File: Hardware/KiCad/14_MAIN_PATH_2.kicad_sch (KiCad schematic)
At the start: 0 parts

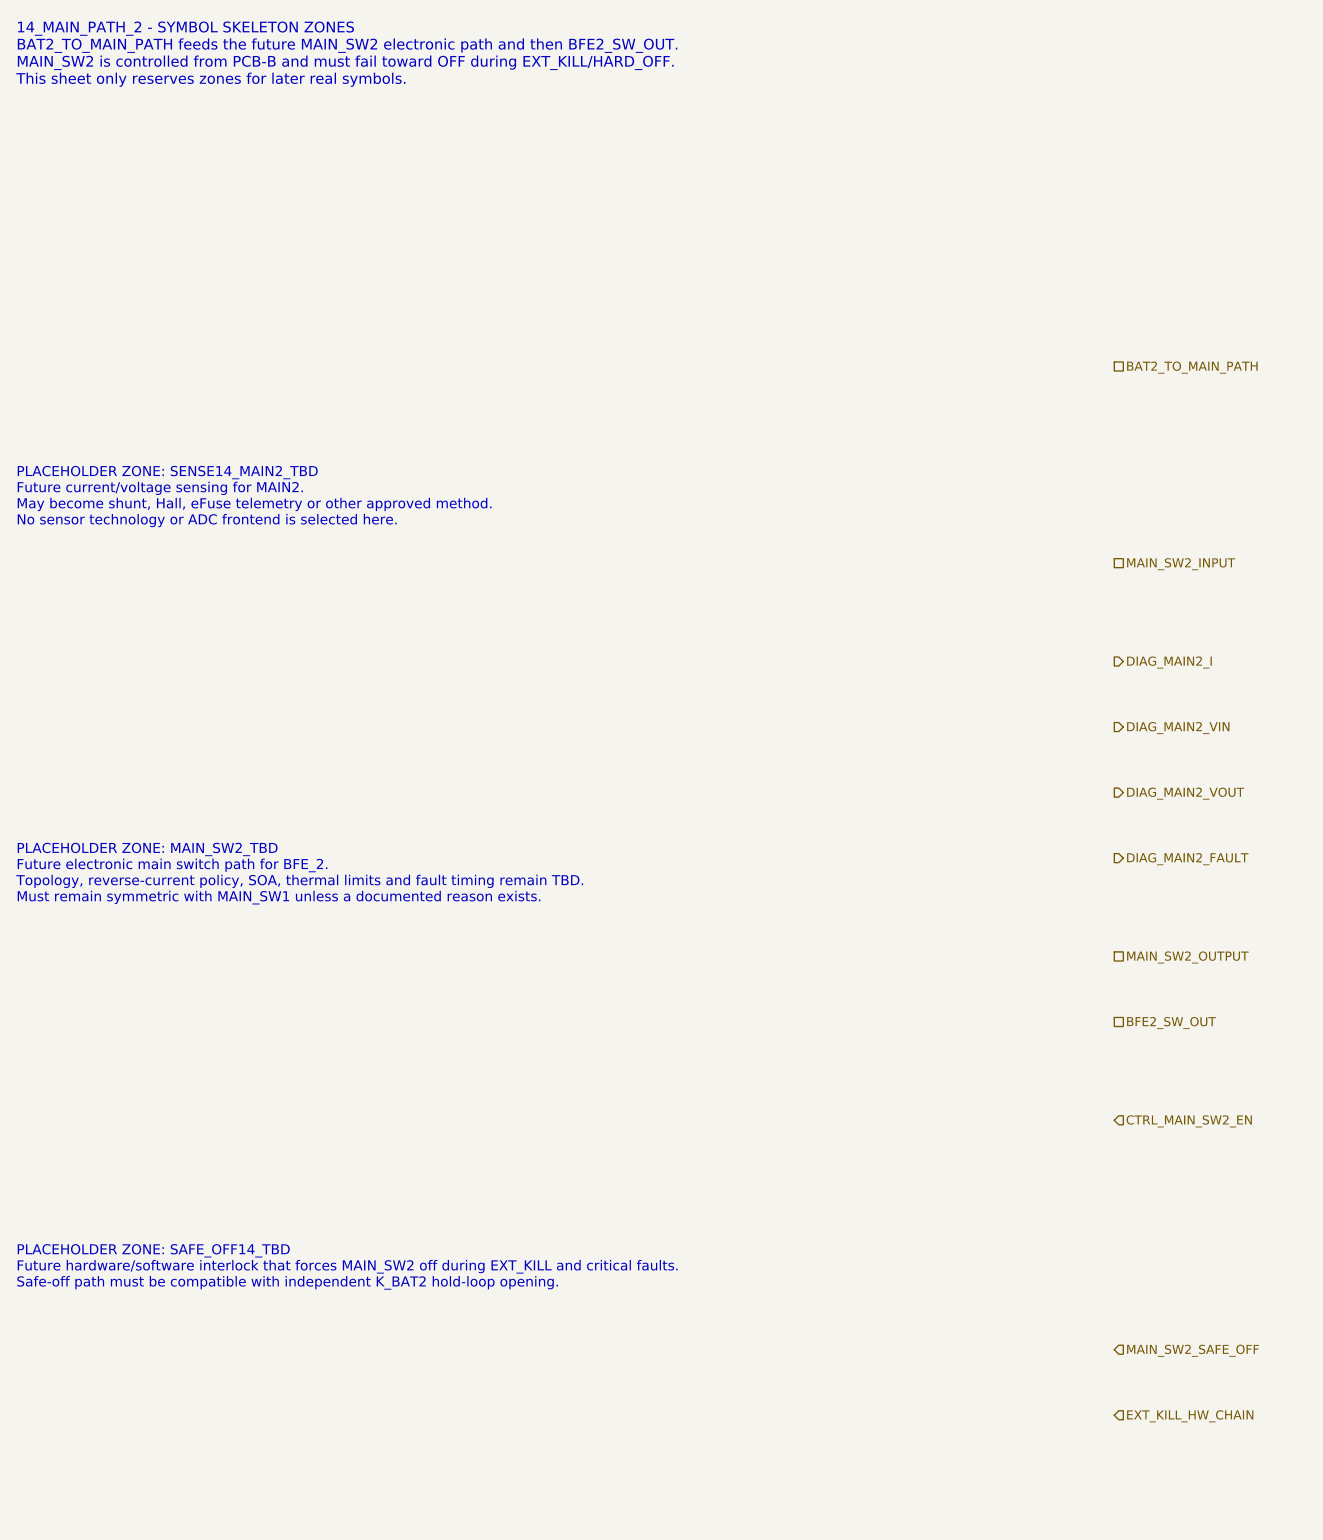
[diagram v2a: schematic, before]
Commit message: hardware: align PCB-B CTRL_RESERVE interfaces
Merge PCB-B interface consistency fixes after verifying canonical names, diagnostics, and independent EXT_KILL final actions.
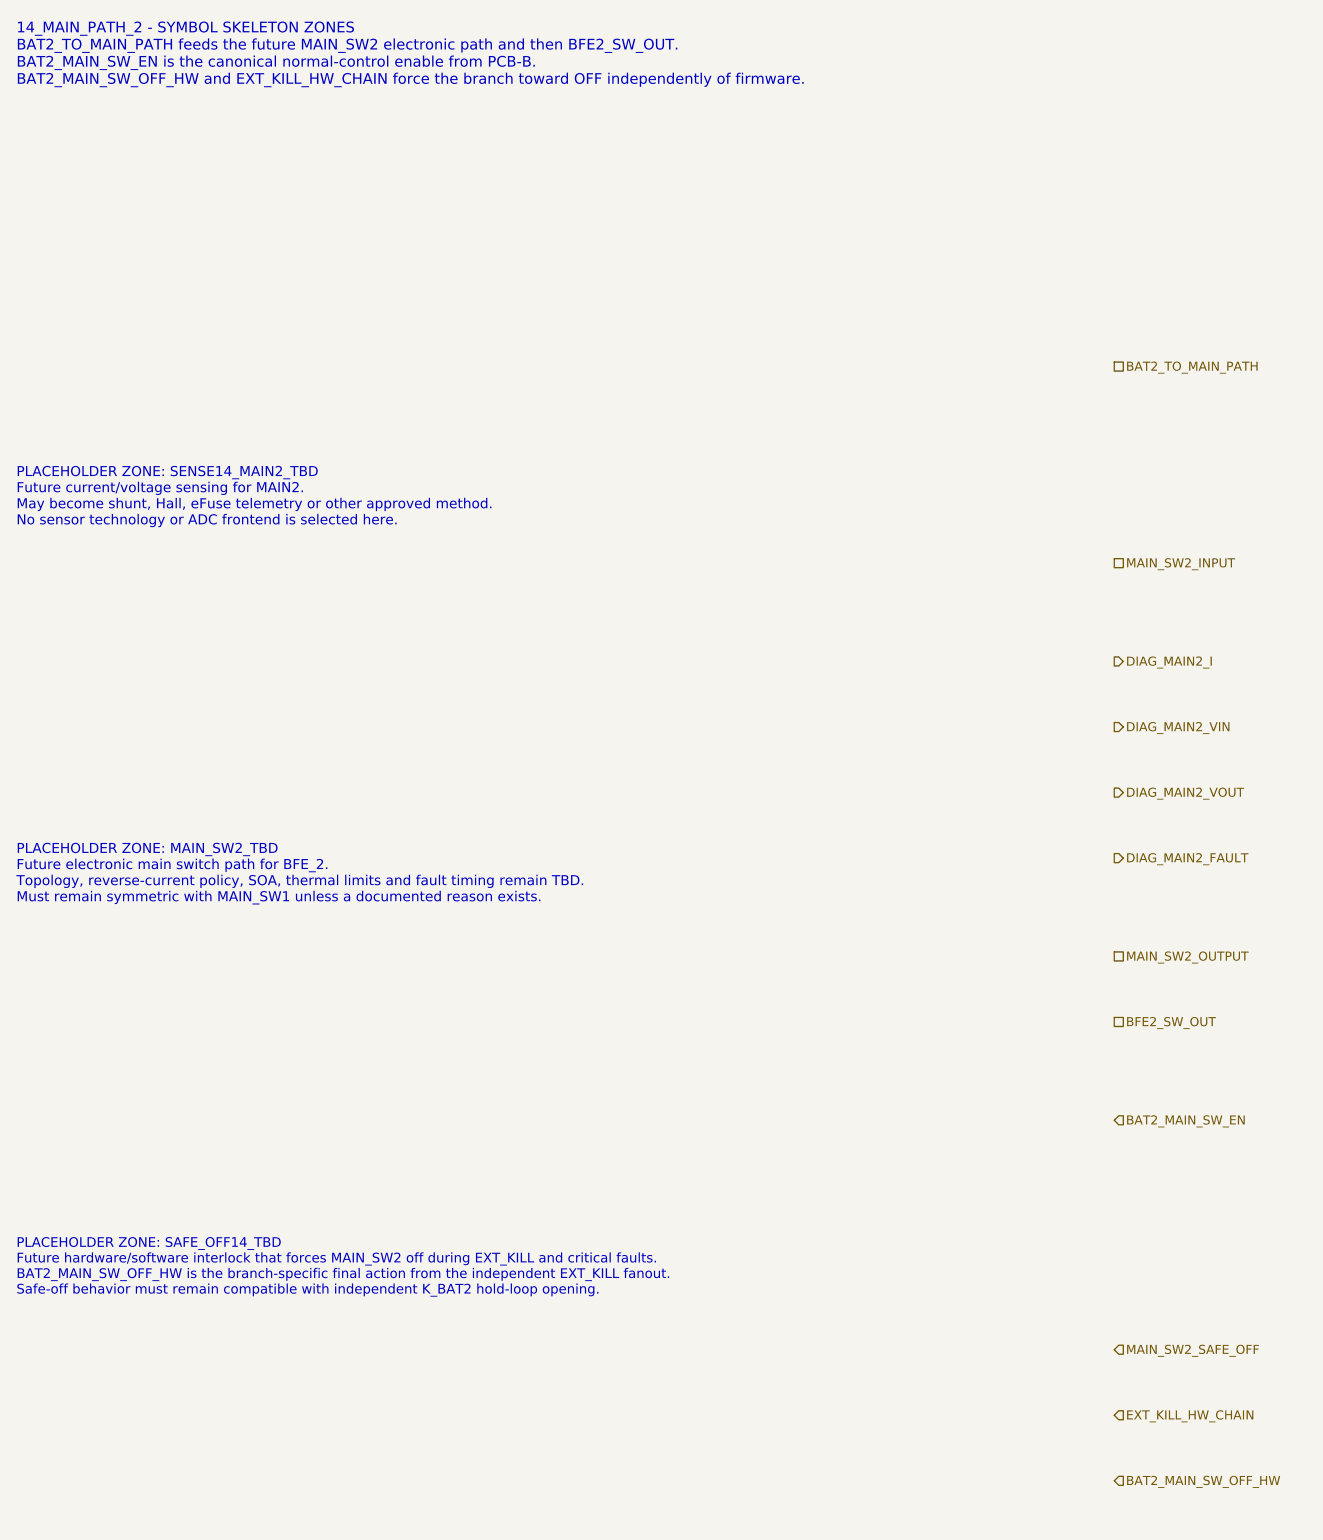
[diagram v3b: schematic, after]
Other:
- note added: "14_MAIN_PATH_2 - SYMBOL SKELETON ZONES BAT2_TO_MAIN_PATH feeds the future MAIN_SW2 electronic path and then BFE2_SW_OUT. BAT2_MAIN_SW_EN is the canonical normal-control enable from PCB-B. BAT2_MAIN_SW_OFF_HW and EXT_KILL_HW_CHAIN force the branch toward OFF independently of firmware."
- note added: "PLACEHOLDER ZONE: SAFE_OFF14_TBD Future hardware/software interlock that forces MAIN_SW2 off during EXT_KILL and critical faults. BAT2_MAIN_SW_OFF_HW is the branch-specific final action from the independent EXT_KILL fanout. Safe-off behavior must remain compatible with independent K_BAT2 hold-loop opening."
- note removed: "14_MAIN_PATH_2 - SYMBOL SKELETON ZONES BAT2_TO_MAIN_PATH feeds the future MAIN_SW2 electronic path and then BFE2_SW_OUT. MAIN_SW2 is controlled from PCB-B and must fail toward OFF during EXT_KILL/HARD_OFF. This sheet only reserves zones for later real symbols."
- note removed: "PLACEHOLDER ZONE: SAFE_OFF14_TBD Future hardware/software interlock that forces MAIN_SW2 off during EXT_KILL and critical faults. Safe-off path must be compatible with independent K_BAT2 hold-loop opening."
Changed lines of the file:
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@@
 		(title "14_MAIN_PATH_2 - BFE_2 main electronic path")
 		(date "2026-07-15")
-		(rev "C1")
+		(rev "C2")
 		(company "Gonoboben/plataVM")
-		(comment 1 "Symbol skeleton: MAIN_SW2, sensing and safe-off placeholders")
+		(comment 1 "Interface consistency: canonical BAT2 main-switch control and hardware-off boundaries")
 		(comment 2 "Symmetric to 13_MAIN_PATH_1; no topology, footprint or component selected")
 	)
-	(text "14_MAIN_PATH_2 - SYMBOL SKELETON ZONES\nBAT2_TO_MAIN_PATH feeds the future MAIN_SW2 electronic path and then BFE2_SW_OUT.\nMAIN_SW2 is controlled from PCB-B and must fail toward OFF during EXT_KILL/HARD_OFF.\nThis sheet only reserves zones for later real symbols."
+	(text "14_MAIN_PATH_2 - SYMBOL SKELETON ZONES\nBAT2_TO_MAIN_PATH feeds the future MAIN_SW2 electronic path and then BFE2_SW_OUT.\nBAT2_MAIN_SW_EN is the canonical normal-control enable from PCB-B.\nBAT2_MAIN_SW_OFF_HW and EXT_KILL_HW_CHAIN force the branch toward OFF independently of firmware."
 		(exclude_from_sim no)
 		(at 12 16 0)
@@
 		(uuid "bfe-lb-00000014-0000-4000-8000-000000000103")
 	)
-	(text "PLACEHOLDER ZONE: SAFE_OFF14_TBD\nFuture hardware/software interlock that forces MAIN_SW2 off during EXT_KILL and critical faults.\nSafe-off path must be compatible with independent K_BAT2 hold-loop opening."
+	(text "PLACEHOLDER ZONE: SAFE_OFF14_TBD\nFuture hardware/software interlock that forces MAIN_SW2 off during EXT_KILL and critical faults.\nBAT2_MAIN_SW_OFF_HW is the branch-specific final action from the independent EXT_KILL fanout.\nSafe-off behavior must remain compatible with independent K_BAT2 hold-loop opening."
 		(exclude_from_sim no)
 		(at 12 164 0)
-		(effects (font (size 1.22 1.22)) (justify left))
+		(effects (font (size 1.18 1.18)) (justify left))
 		(uuid "bfe-lb-00000014-0000-4000-8000-000000000104")
 	)
@@
 	(hierarchical_label "MAIN_SW2_OUTPUT" (shape passive) (exclude_from_sim no) (at 146 126 0) (effects (font (size 1.1 1.1)) (justify left)) (uuid "bfe-lb-00000014-0000-4000-8000-000000000203"))
 	(hierarchical_label "BFE2_SW_OUT" (shape passive) (exclude_from_sim no) (at 146 134 0) (effects (font (size 1.1 1.1)) (justify left)) (uuid "bfe-lb-00000014-0000-4000-8000-000000000204"))
-	(hierarchical_label "CTRL_MAIN_SW2_EN" (shape input) (exclude_from_sim no) (at 146 146 0) (effects (font (size 1.1 1.1)) (justify left)) (uuid "bfe-lb-00000014-0000-4000-8000-000000000205"))
+	(hierarchical_label "BAT2_MAIN_SW_EN" (shape input) (exclude_from_sim no) (at 146 146 0) (effects (font (size 1.1 1.1)) (justify left)) (uuid "bfe-lb-00000014-0000-4000-8000-000000000205"))
 	(hierarchical_label "MAIN_SW2_SAFE_OFF" (shape input) (exclude_from_sim no) (at 146 174 0) (effects (font (size 1.1 1.1)) (justify left)) (uuid "bfe-lb-00000014-0000-4000-8000-000000000206"))
 	(hierarchical_label "EXT_KILL_HW_CHAIN" (shape input) (exclude_from_sim no) (at 146 182 0) (effects (font (size 1.1 1.1)) (justify left)) (uuid "bfe-lb-00000014-0000-4000-8000-000000000207"))
+	(hierarchical_label "BAT2_MAIN_SW_OFF_HW" (shape input) (exclude_from_sim no) (at 146 190 0) (effects (font (size 1.1 1.1)) (justify left)) (uuid "bfe-lb-00000014-0000-4000-8000-000000000212"))
 	(hierarchical_label "DIAG_MAIN2_I" (shape output) (exclude_from_sim no) (at 146 90 0) (effects (font (size 1.1 1.1)) (justify left)) (uuid "bfe-lb-00000014-0000-4000-8000-000000000208"))
 	(hierarchical_label "DIAG_MAIN2_VIN" (shape output) (exclude_from_sim no) (at 146 98 0) (effects (font (size 1.1 1.1)) (justify left)) (uuid "bfe-lb-00000014-0000-4000-8000-000000000209"))
